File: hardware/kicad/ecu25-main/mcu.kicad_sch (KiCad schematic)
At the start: 29 parts, among them J11 TC2030 SWD, J14 DEBUG_UART, U12 STM32F407VGT6, Y1 8MHz, Y2 32.768kHz

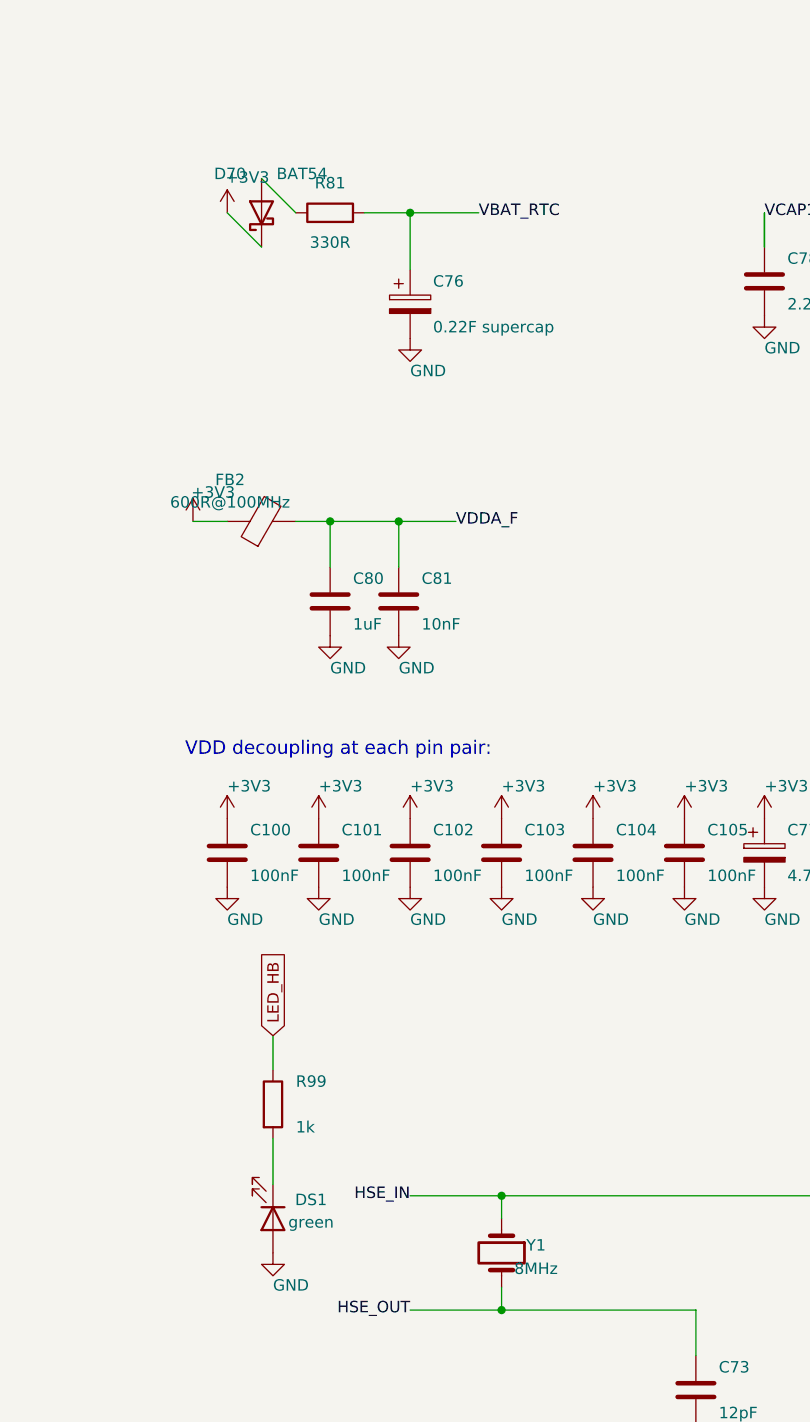
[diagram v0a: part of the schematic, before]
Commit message: Fix SME review findings: 3 critical, 6 major schematic faults
Critical:
- RON pin no longer shorted to GND (R4 moved off C3's column)
- LM2903 MPU comparator +/- inputs unmerged (separate route columns)
- Supercap charge diode D70 un-reversed (anode to +3V3)

Major:
- Buck UVLO divider restored (stray EN stub ended on C3 column = EN
  tied to +24V; stub removed)
- RS485 fail-safe bias polarity corrected (pull-up A, pull-down B)
- U8 spare op-amp unit placed and tied off (was floating on VREF die)
- Heartbeat LED DS1 un-reversed
- VREF_MID buffer dual feedback added (R93 DC path + C93 AC path)
- D80 value SMBJ33A -> SMBJ33CA (bidirectional, matches symbol)

Added netlist-level sweep check (shorted 2-pin devices, rail
membership) since the geometric tracer is blind to shorts closed
through power symbols across wire islands. Sweep: CLEAN, 0 issues.
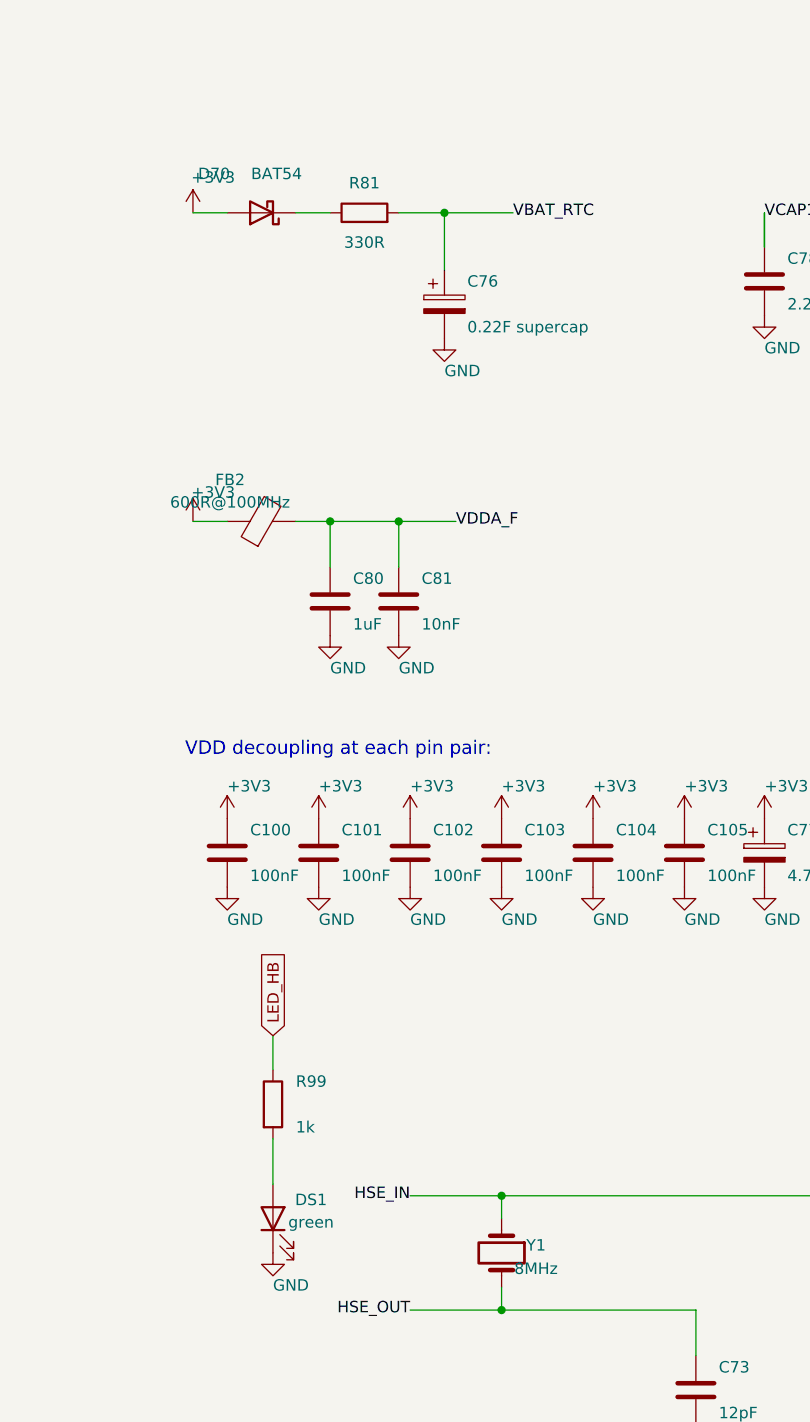
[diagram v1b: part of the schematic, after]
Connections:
- net +3V3: now also D70.2 (A); no longer D70.1 (K)
- net GND: now also DS1.1 (K); no longer DS1.2 (A)
- net at R99.2: now also DS1.2 (A); no longer DS1.1 (K)
- net at R81.1: now also D70.1 (K); no longer D70.2 (A)

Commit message: Assign footprints to all 299 components in schematic generator
- By-ref exceptions + per-symbol defaults + value rules (wattage/voltage classes)
- Field connectors: MKDS-3 for battery/AC/CT/relay terminals, MKDS-1,5 for signal
- Q1 reverse-protection FET: Q_PMOS_GSD -> Q_PMOS_GDS + TO-252-2 (DPAK pad
  numbering 1=G 2=D 3=S; GSD variant would swap D/S in the netlist), part
  SQD50P06-15L
- Verified: all footprint files exist in KiCad 7 libs, all symbol pin numbers
  present in footprint pads, netlist sweep still clean
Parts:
- C100, C101, C102, C103, C104, C105, C71, C72, C73, C74, C75, C78, C79, C80, C81: footprint (none) -> Capacitor_SMD:C_0603_1608Metric
- C76: footprint (none) -> Capacitor_THT:CP_Radial_D10.0mm_P5.00mm
- C77: footprint (none) -> Capacitor_SMD:CP_Elec_4x5.4
- D70: footprint (none) -> Diode_SMD:D_SOD-123
- DS1: footprint (none) -> LED_SMD:LED_0805_2012Metric
- FB2: footprint (none) -> Inductor_SMD:L_0603_1608Metric
- J11: footprint (none) -> Connector:Tag-Connect_TC2030-IDC-NL_2x03_P1.27mm_Vertical
- J14: footprint (none) -> Connector_PinHeader_2.54mm:PinHeader_1x03_P2.54mm_Vertical
- JP3: footprint (none) -> Jumper:SolderJumper-2_P1.3mm_Open_RoundedPad1.0x1.5mm
- R80, R81, R99: footprint (none) -> Resistor_SMD:R_0603_1608Metric
- U12: footprint (none) -> Package_QFP:LQFP-100_14x14mm_P0.5mm
- Y1: footprint (none) -> Crystal:Crystal_SMD_HC49-SD
- Y2: footprint (none) -> Crystal:Crystal_SMD_3215-2Pin_3.2x1.5mm
